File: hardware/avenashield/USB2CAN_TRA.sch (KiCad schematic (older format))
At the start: 29 parts, among them U4 STM32F042C6Tx, U5 MCP2551-I-SN, U9 TXS0102DCT, Y2 16 MHz

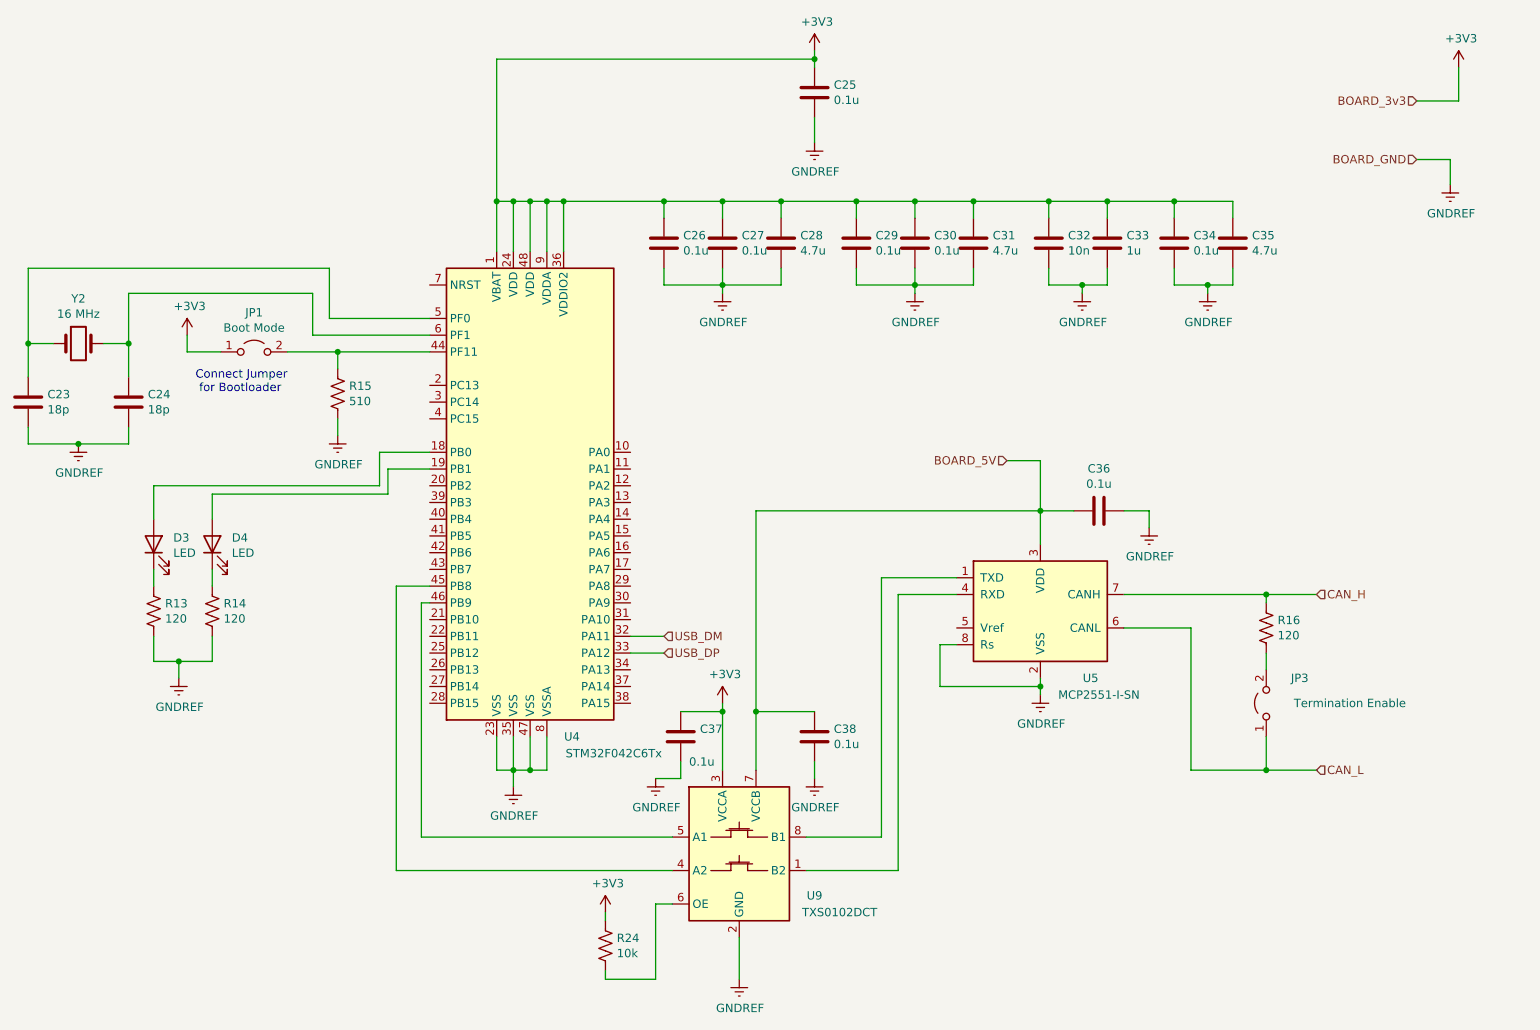
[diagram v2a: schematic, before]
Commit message: Improved I2C bus routing
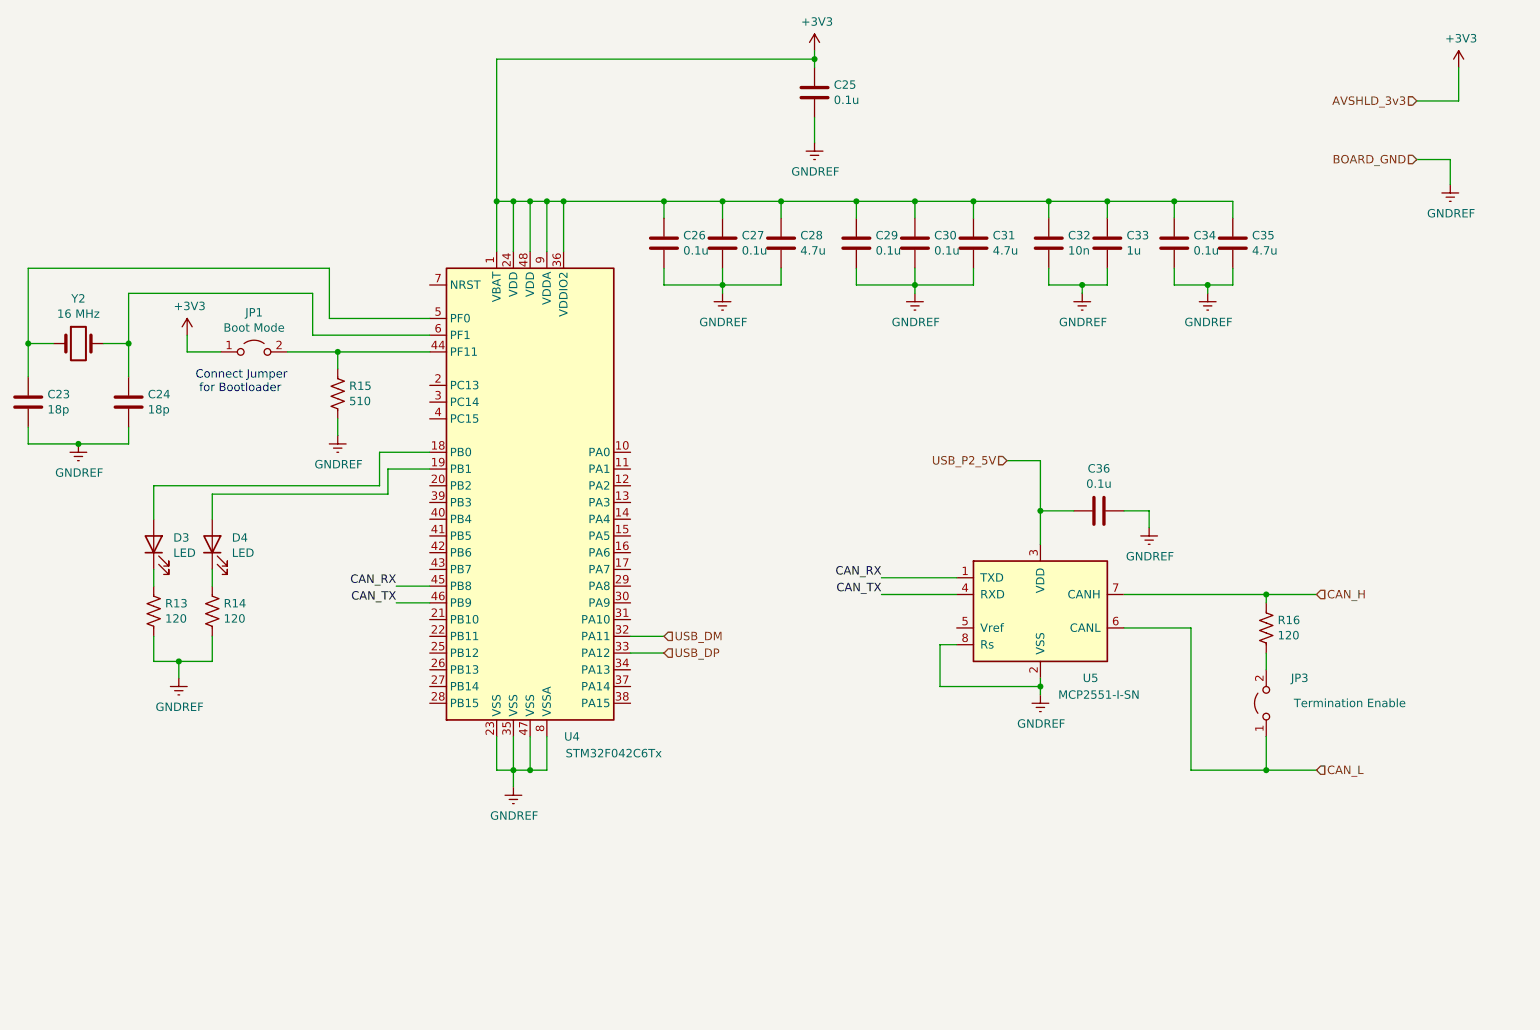
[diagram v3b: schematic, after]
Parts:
- removed C37, C38: 0.1u, Capacitor_SMD:C_0805_2012Metric_Pad1.15x1.40mm_HandSolder, symbol Device:C
- removed R24: 10k, Resistor_SMD:R_0805_2012Metric_Pad1.15x1.40mm_HandSolder, symbol Device:R_US
- removed U9: TXS0102DCT, Package_SO:SSOP-8_2.95x2.8mm_P0.65mm, symbol Logic_LevelTranslator:TXS0102DCT
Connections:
- net CAN_RX: now reaches U4.45 (PB8)
- net CAN_RX: now also U5.1 (TXD)
- net CAN_TX: now reaches U4.46 (PB9)
- net CAN_TX: now also U5.4 (RXD)
- net BOARD_5V renamed USB_P2_5V
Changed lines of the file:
@@
 Wire Wire Line
 	3750 4000 3550 4000
-Wire Wire Line
-	3750 4100 3700 4100
-Wire Wire Line
-	3700 4100 3700 5500
 $Comp
 L Jumper:Jumper_2_Open JP1
@@
 $EndComp
 Text HLabel 9650 1100 0    50   Input ~ 0
-BOARD_3v3
+AVSHLD_3v3
 Text HLabel 7200 3250 0    50   Input ~ 0
-BOARD_5V
+USB_P2_5V
 Wire Wire Line
 	9650 1100 9900 1100
@@
 Wire Wire Line
 	8750 4900 8750 5100
-$Comp
-L Logic_LevelTranslator:TXS0102DCT U9
-U 1 1 5E61F145
-P 5600 5600
-F 0 "U9" H 6050 5350 50  0000 C CNN
-F 1 "TXS0102DCT" H 6200 5250 50  0000 C CNN
-F 2 "Package_SO:SSOP-8_2.95x2.8mm_P0.65mm" H 5600 5050 50  0001 C CNN
-F 3 "http://www.ti.com/lit/gpn/txs0102" H 5600 5580 50  0001 C CNN
-	1    5600 5600
-	1    0    0    -1
-$EndComp
-Wire Wire Line
-	5200 5500 3700 5500
-Wire Wire Line
-	3550 5700 5200 5700
-Wire Wire Line
-	3550 4000 3550 5700
-$Comp
-L power:+3V3 #PWR0184
-U 1 1 5E63D55D
-P 5500 4700
-F 0 "#PWR0184" H 5500 4550 50  0001 C CNN
-F 1 "+3V3" H 5515 4873 50  0000 C CNN
-F 2 "" H 5500 4700 50  0001 C CNN
-F 3 "" H 5500 4700 50  0001 C CNN
-	1    5500 4700
-	1    0    0    -1
-$EndComp
-Wire Wire Line
-	5500 4700 5500 4750
-$Comp
-L Device:C C38
-U 1 1 5E648F7D
-P 6050 4900
-F 0 "C38" H 6165 4946 50  0000 L CNN
-F 1 "0.1u" H 6165 4855 50  0000 L CNN
-F 2 "Capacitor_SMD:C_0805_2012Metric_Pad1.15x1.40mm_HandSolder" H 6088 4750 50  0001 C CNN
-F 3 "~" H 6050 4900 50  0001 C CNN
-	1    6050 4900
-	1    0    0    -1
-$EndComp
-Connection ~ 5700 4750
-Wire Wire Line
-	5700 4750 5700 5100
-$Comp
-L Device:C C37
-U 1 1 5E64F0D2
-P 5250 4900
-F 0 "C37" H 5365 4946 50  0000 L CNN
-F 1 "0.1u" H 5300 4750 50  0000 L CNN
-F 2 "Capacitor_SMD:C_0805_2012Metric_Pad1.15x1.40mm_HandSolder" H 5288 4750 50  0001 C CNN
-F 3 "~" H 5250 4900 50  0001 C CNN
-	1    5250 4900
-	1    0    0    -1
-$EndComp
-Wire Wire Line
-	5250 4750 5500 4750
-Connection ~ 5500 4750
-Wire Wire Line
-	5500 4750 5500 5100
-$Comp
-L power:GNDREF #PWR0185
-U 1 1 5E655495
-P 5100 5150
-AR Path="/5E564EEA/5E655495" Ref="#PWR0185"  Part="1"
-AR Path="/5E45C906/5E655495" Ref="#PWR?"  Part="1"
-F 0 "#PWR0185" H 5100 4900 50  0001 C CNN
-F 1 "GNDREF" H 5105 4977 50  0000 C CNN
-F 2 "" H 5100 5150 50  0001 C CNN
-F 3 "" H 5100 5150 50  0001 C CNN
-	1    5100 5150
-	1    0    0    -1
-$EndComp
-Wire Wire Line
-	5100 5150 5250 5150
-Wire Wire Line
-	5250 5150 5250 5050
-$Comp
-L power:GNDREF #PWR0186
-U 1 1 5E65BAE2
-P 6050 5150
-AR Path="/5E564EEA/5E65BAE2" Ref="#PWR0186"  Part="1"
-AR Path="/5E45C906/5E65BAE2" Ref="#PWR?"  Part="1"
-F 0 "#PWR0186" H 6050 4900 50  0001 C CNN
-F 1 "GNDREF" H 6055 4977 50  0000 C CNN
-F 2 "" H 6050 5150 50  0001 C CNN
-F 3 "" H 6050 5150 50  0001 C CNN
-	1    6050 5150
-	1    0    0    -1
-$EndComp
-Wire Wire Line
-	6550 5700 6550 4050
-Wire Wire Line
-	6000 5700 6550 5700
-Wire Wire Line
-	6550 4050 6900 4050
-Wire Wire Line
-	6450 5500 6450 3950
-Wire Wire Line
-	6000 5500 6450 5500
 Wire Wire Line
 	6450 3950 6900 3950
 Wire Wire Line
-	5700 4750 6050 4750
-Wire Wire Line
-	6050 5050 6050 5150
-$Comp
-L Device:R_US R24
-U 1 1 5E6856CF
-P 4800 6150
-F 0 "R24" H 4732 6104 50  0000 R CNN
-F 1 "10k" H 4732 6195 50  0000 R CNN
-F 2 "Resistor_SMD:R_0805_2012Metric_Pad1.15x1.40mm_HandSolder" V 4840 6140 50  0001 C CNN
-F 3 "~" H 4800 6150 50  0001 C CNN
-	1    4800 6150
-	-1   0    0    1
-$EndComp
-$Comp
-L power:+3V3 #PWR0187
-U 1 1 5E6965E3
-P 4800 5950
-F 0 "#PWR0187" H 4800 5800 50  0001 C CNN
-F 1 "+3V3" H 4815 6123 50  0000 C CNN
-F 2 "" H 4800 5950 50  0001 C CNN
-F 3 "" H 4800 5950 50  0001 C CNN
-	1    4800 5950
-	1    0    0    -1
-$EndComp
-Wire Wire Line
-	4800 5950 4800 6000
-Wire Wire Line
-	4800 6300 4800 6350
-Wire Wire Line
-	4800 6350 5100 6350
-Wire Wire Line
-	5100 6350 5100 5900
-Wire Wire Line
-	5100 5900 5200 5900
-$Comp
-L power:GNDREF #PWR0195
-U 1 1 5E715CCE
-P 5600 6350
-AR Path="/5E564EEA/5E715CCE" Ref="#PWR0195"  Part="1"
-AR Path="/5E45C906/5E715CCE" Ref="#PWR?"  Part="1"
-F 0 "#PWR0195" H 5600 6100 50  0001 C CNN
-F 1 "GNDREF" H 5605 6177 50  0000 C CNN
-F 2 "" H 5600 6350 50  0001 C CNN
-F 3 "" H 5600 6350 50  0001 C CNN
-	1    5600 6350
-	1    0    0    -1
-$EndComp
-Wire Wire Line
-	5600 6350 5600 6100
-Wire Wire Line
 	7200 3250 7400 3250
 Wire Wire Line
 	7400 3250 7400 3550
 Wire Wire Line
-	5700 3550 7400 3550
-Wire Wire Line
-	5700 3550 5700 4750
+	3550 4100 3750 4100
+Text Label 3550 4000 2    50   ~ 0
+CAN_RX
+Text Label 3550 4100 2    50   ~ 0
+CAN_TX
+Text Label 6450 3950 2    50   ~ 0
+CAN_RX
+Text Label 6450 4050 2    50   ~ 0
+CAN_TX
+Wire Wire Line
+	6450 4050 6900 4050
 $EndSCHEMATC
